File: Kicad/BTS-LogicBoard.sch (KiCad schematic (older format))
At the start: 49 parts, among them J1 Conn_01x06, J2 Conn_01x04, J3 Conn_01x02, Q1 BC817, Q2 BC807, Q3 BC817, Q4 BC807, Q5 BC817, SW1 SW_DPDT_x2, SW2 SW_DPDT_x2, U1 NCS2252SN2T1G, U2 NE555D, U3 NCS2252SN2T1G

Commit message: Started routing
Signed-off-by: Benoit Tarrade <btarrade@slb.com>
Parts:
- removed C8: 470uF, Capacitor_SMD:CP_Elec_10x10, symbol Device:C
- added C8: 470uF, Capacitor_SMD:CP_Elec_10x10, symbol Device:CP
- H1, H2, H3, H4: renamed from H?; footprint (none) -> MountingHole:MountingHole_3.2mm_M3_DIN965_Pad_TopBottom
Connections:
- net GND: now also C8.2
- net at Q4.3 (C), R14.2, U3.4 (In-): now also C8.1
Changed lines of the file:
@@
 	0    1    1    0
-$EndComp
-$Comp
-L Device:C C8
-U 1 1 613EB2E3
-P 6350 1975
-F 0 "C8" H 6605 1985 50  0000 R CNN
-F 1 "470uF" H 6625 2090 50  0000 R CNN
-F 2 "Capacitor_SMD:CP_Elec_10x10" H 6388 1825 50  0001 C CNN
-F 3 "~" H 6350 1975 50  0001 C CNN
-	1    6350 1975
-	-1   0    0    1
 $EndComp
 Text Label 5750 1500 2    50   ~ 0
@@
 This configuration allows the capacitor\nto charge up quickly when PWM is enabled (charged up in \nfew µseconds) and discharge very slowly through the\n390k resistor. Like so, cooling fans will stay on for about\n2 minutes after the modules are shut off, so that we are \ntaking care of the thermal inertia of the modules.
 $Comp
-L Mechanical:MountingHole_Pad H?
+L Mechanical:MountingHole_Pad H1
 U 1 1 61480724
 P 6250 4275
-F 0 "H?" V 6487 4278 50  0000 C CNN
+F 0 "H1" V 6487 4278 50  0000 C CNN
 F 1 "MountingHole_Pad" V 6396 4278 50  0000 C CNN
-F 2 "" H 6250 4275 50  0001 C CNN
+F 2 "MountingHole:MountingHole_3.2mm_M3_DIN965_Pad_TopBottom" H 6250 4275 50  0001 C CNN
 F 3 "~" H 6250 4275 50  0001 C CNN
 	1    6250 4275
@@
 $EndComp
 $Comp
-L power:GND #PWR?
+L power:GND #PWR09
 U 1 1 61480D81
 P 6350 4275
-F 0 "#PWR?" H 6350 4025 50  0001 C CNN
+F 0 "#PWR09" H 6350 4025 50  0001 C CNN
 F 1 "GND" H 6355 4102 50  0000 C CNN
 F 2 "" H 6350 4275 50  0001 C CNN
@@
 $EndComp
 $Comp
-L Mechanical:MountingHole_Pad H?
+L Mechanical:MountingHole_Pad H2
 U 1 1 614814C8
 P 6250 4550
-F 0 "H?" V 6487 4553 50  0000 C CNN
+F 0 "H2" V 6487 4553 50  0000 C CNN
 F 1 "MountingHole_Pad" V 6396 4553 50  0000 C CNN
-F 2 "" H 6250 4550 50  0001 C CNN
+F 2 "MountingHole:MountingHole_3.2mm_M3_DIN965_Pad_TopBottom" H 6250 4550 50  0001 C CNN
 F 3 "~" H 6250 4550 50  0001 C CNN
 	1    6250 4550
@@
 $EndComp
 $Comp
-L power:GND #PWR?
+L power:GND #PWR010
 U 1 1 614814CE
 P 6350 4550
-F 0 "#PWR?" H 6350 4300 50  0001 C CNN
+F 0 "#PWR010" H 6350 4300 50  0001 C CNN
 F 1 "GND" H 6355 4377 50  0000 C CNN
 F 2 "" H 6350 4550 50  0001 C CNN
@@
 $EndComp
 $Comp
-L Mechanical:MountingHole_Pad H?
+L Mechanical:MountingHole_Pad H3
 U 1 1 61484F71
 P 6250 4800
-F 0 "H?" V 6487 4803 50  0000 C CNN
+F 0 "H3" V 6487 4803 50  0000 C CNN
 F 1 "MountingHole_Pad" V 6396 4803 50  0000 C CNN
-F 2 "" H 6250 4800 50  0001 C CNN
+F 2 "MountingHole:MountingHole_3.2mm_M3_DIN965_Pad_TopBottom" H 6250 4800 50  0001 C CNN
 F 3 "~" H 6250 4800 50  0001 C CNN
 	1    6250 4800
@@
 $EndComp
 $Comp
-L power:GND #PWR?
+L power:GND #PWR011
 U 1 1 61484F77
 P 6350 4800
-F 0 "#PWR?" H 6350 4550 50  0001 C CNN
+F 0 "#PWR011" H 6350 4550 50  0001 C CNN
 F 1 "GND" H 6355 4627 50  0000 C CNN
 F 2 "" H 6350 4800 50  0001 C CNN
@@
 $EndComp
 $Comp
-L Mechanical:MountingHole_Pad H?
+L Mechanical:MountingHole_Pad H4
 U 1 1 61488E72
 P 6250 5050
-F 0 "H?" V 6487 5053 50  0000 C CNN
+F 0 "H4" V 6487 5053 50  0000 C CNN
 F 1 "MountingHole_Pad" V 6396 5053 50  0000 C CNN
-F 2 "" H 6250 5050 50  0001 C CNN
+F 2 "MountingHole:MountingHole_3.2mm_M3_DIN965_Pad_TopBottom" H 6250 5050 50  0001 C CNN
 F 3 "~" H 6250 5050 50  0001 C CNN
 	1    6250 5050
@@
 $EndComp
 $Comp
-L power:GND #PWR?
+L power:GND #PWR012
 U 1 1 61488E78
 P 6350 5050
-F 0 "#PWR?" H 6350 4800 50  0001 C CNN
+F 0 "#PWR012" H 6350 4800 50  0001 C CNN
 F 1 "GND" H 6355 4877 50  0000 C CNN
 F 2 "" H 6350 5050 50  0001 C CNN
@@
 	0    -1   -1   0
 $EndComp
+$Comp
+L Device:CP C8
+U 1 1 614D139C
+P 6350 1975
+F 0 "C8" H 6468 2021 50  0000 L CNN
+F 1 "470uF" H 6468 1930 50  0000 L CNN
+F 2 "Capacitor_SMD:CP_Elec_10x10" H 6388 1825 50  0001 C CNN
+F 3 "~" H 6350 1975 50  0001 C CNN
+	1    6350 1975
+	1    0    0    -1
+$EndComp
 $EndSCHEMATC

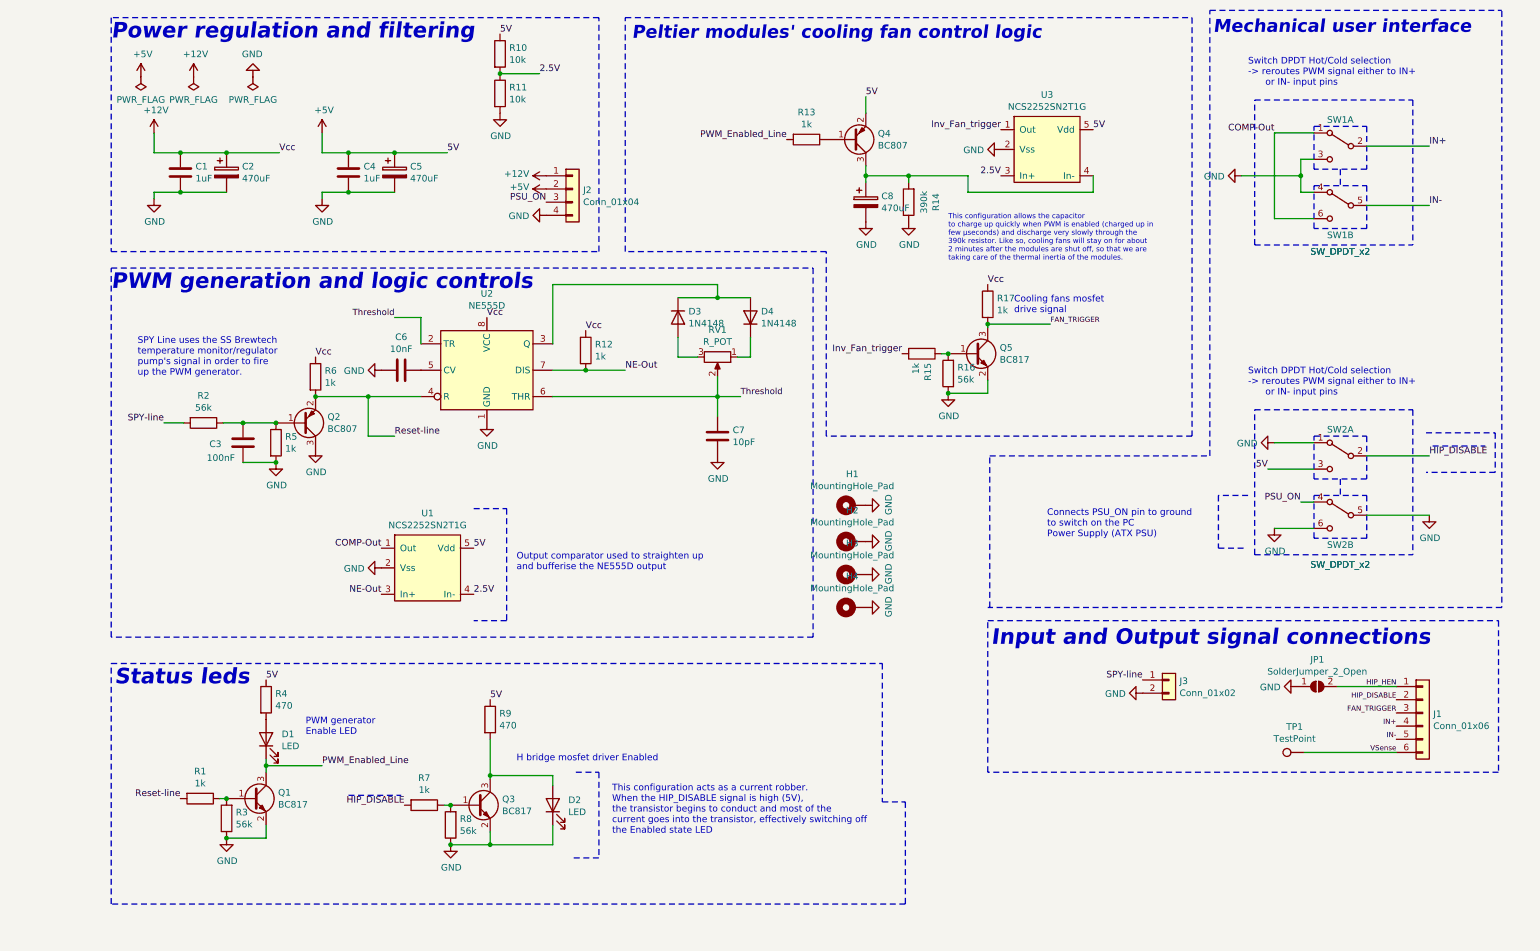
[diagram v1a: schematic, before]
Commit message: Added NE555 enable override by HIP_DISABLE signal
Signed-off-by: Benoit Tarrade <btarrade@slb.com>
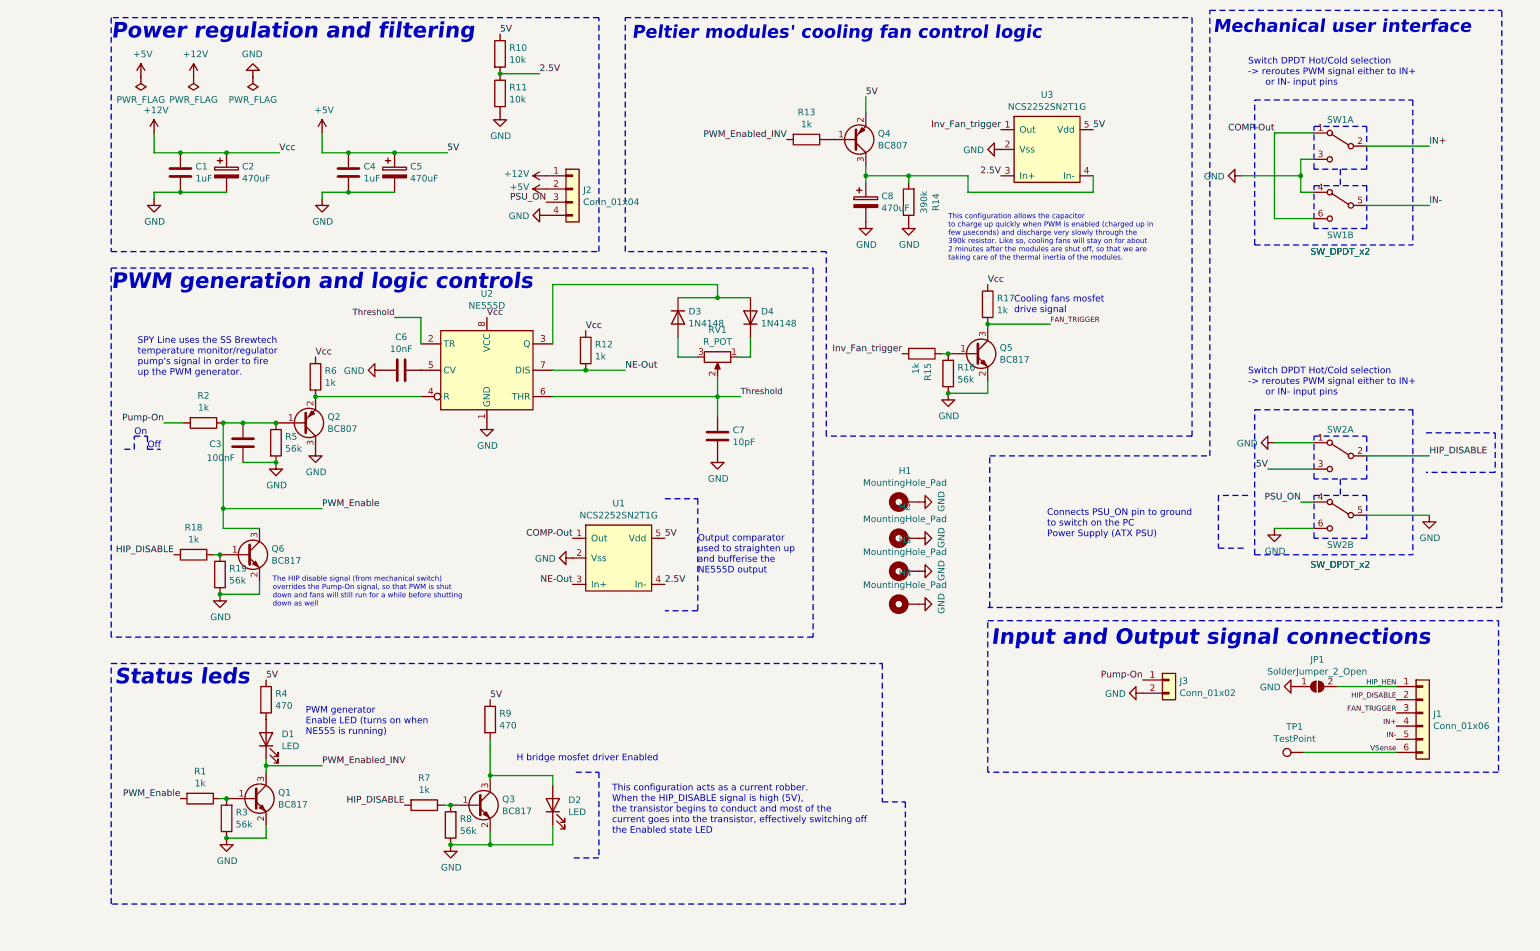
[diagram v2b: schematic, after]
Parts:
- added Q6: BC817, Package_TO_SOT_SMD:SOT-23, symbol Transistor_BJT:BC817
- added R18: 1k, Resistor_SMD:R_1206_3216Metric_Pad1.30x1.75mm_HandSolder, symbol Device:R
- added R19: 56k, Resistor_SMD:R_1206_3216Metric_Pad1.30x1.75mm_HandSolder, symbol Device:R
- R2: value 56k -> 1k
- R5: value 1k -> 56k
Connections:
- net GND: now also Q6.2 (E), R19.1
- net HIP_DISABLE: now also R18.2
- net PWM_Enable: now reaches C3.2, Q2.1 (B), R2.1, R5.1
- net PWM_Enable: now also R1.2, Q6.3 (C)
- net PWM_Enabled_Line renamed PWM_Enabled_INV
- net Reset-line: no longer names the net of Q2.2 (E), R6.2, U2.4 (R)
- net Reset-line: no longer R1.2
- net SPY-line renamed Pump-On
- new net: Q6.1 (B), R18.1, R19.2
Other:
- note added: "Off"
- note added: "On"
- note added: "Output comparator \nused to straighten up \nand bufferise the \nNE555D output"
- note added: "PWM generator \nEnable LED (turns on when \nNE555 is running)"
- note added: "The HIP disable signal (from mechanical switch)\noverrides the Pump-On signal, so that PWM is shut\ndown and fans will still run for a while before shutting\ndown as well"
- note removed: "Output comparator used to straighten up \nand bufferise the NE555D output"
- note removed: "PWM generator \nEnable LED"
- moved on the sheet: H1, H2, H3, H4, U1

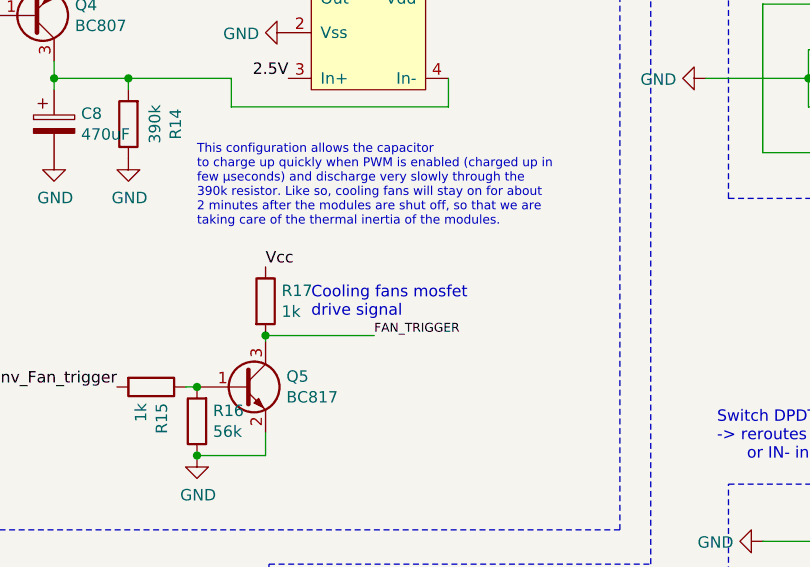
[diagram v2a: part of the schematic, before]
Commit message: Fan trigger now uses 5V instead of 12v to prevent blowing up fans mosfets
Signed-off-by: bebenlebricolo <benoittarrade@hotmail.fr>
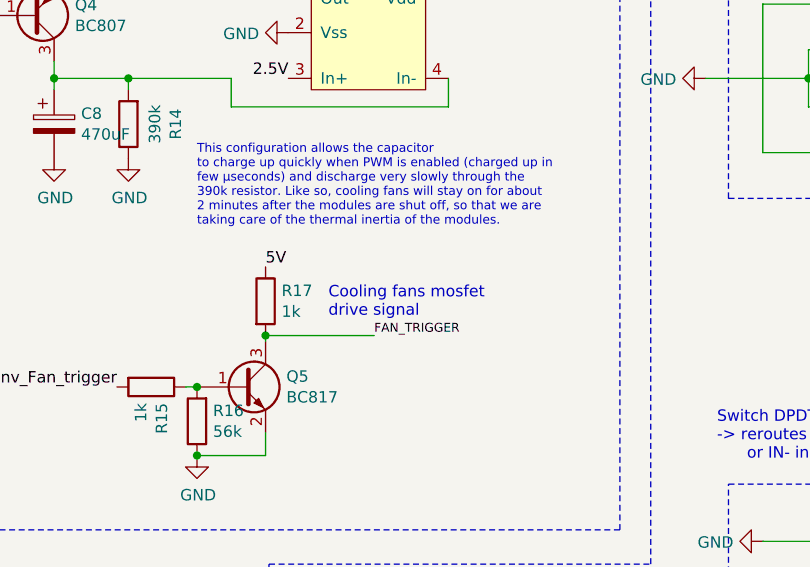
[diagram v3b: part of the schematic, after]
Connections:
- net +12V: no longer R17.1
- net +5V: now also R17.1
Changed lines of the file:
@@
 	7275 3425 7275 3325
 Connection ~ 6975 3425
-Text Notes 7475 2825 0    50   ~ 0
+Text Notes 7550 2825 0    50   ~ 0
 Cooling fans mosfet \ndrive signal
 Wire Wire Line
@@
 	7275 2900 7275 2925
 Connection ~ 7275 2900
-Text Label 7275 2600 0    50   ~ 0
-Vcc
 Text Label 6350 1175 0    50   ~ 0
 5V
@@
 Text Label 1150 6500 2    50   ~ 0
 PWM_Enable
+Text Label 7275 2600 0    50   ~ 0
+5V
 $EndSCHEMATC
